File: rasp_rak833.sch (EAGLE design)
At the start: 22 parts, among them IC1 SHTC3, IC2 AMS1117-3.3, K1 PIN20X2

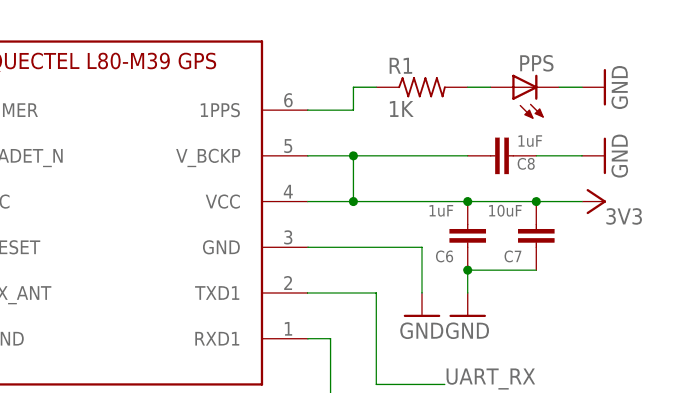
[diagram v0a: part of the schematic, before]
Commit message: Board tested. Minor resistor value tweaks
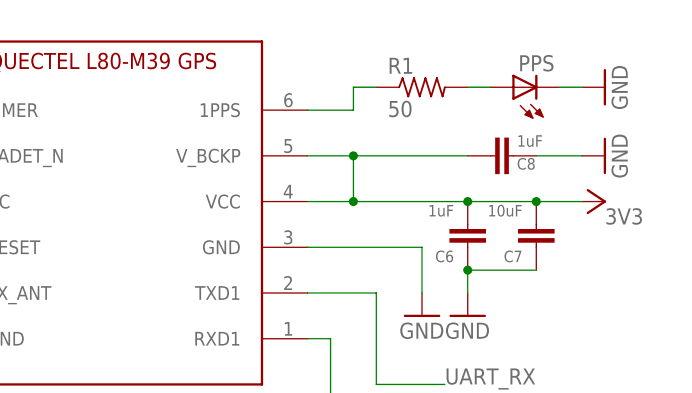
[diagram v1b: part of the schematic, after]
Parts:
- R1: value 1K -> 50
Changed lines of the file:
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@@
 <part name="GND4" library="supply1" library_urn="urn:adsk.eagle:library:371" deviceset="GND" device=""/>
 <part name="PPS" library="adafruit" library_urn="urn:adsk.eagle:library:420" deviceset="LED" device="CHIP-LED0805"/>
-<part name="R1" library="adafruit" library_urn="urn:adsk.eagle:library:420" deviceset="R-US_" device="R0805" value="1K"/>
+<part name="R1" library="adafruit" library_urn="urn:adsk.eagle:library:420" deviceset="R-US_" device="R0805" value="50"/>
 <part name="GND5" library="supply1" library_urn="urn:adsk.eagle:library:371" deviceset="GND" device=""/>
 <part name="C3" library="xose" deviceset="C-EU" device="0805" value="1uF"/>
